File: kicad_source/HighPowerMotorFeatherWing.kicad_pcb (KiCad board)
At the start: 2 copper layers, 100 x 60 mm, 97 parts, among them CN1 ADAFRUIT_FEATHER, P1 WR-TBL_691313710002, P2 WR-TBL_691322310002, P3 WR-TBL_691313710002, P4 WR-TBL_691313710002, Q1 Q_NPN_BEC, Q2 IPD90P03P4L- 04, U1 IFX007T, U2 74xx08, U3 IFX007T, U4 IFX007T, U5 IFX007T, U6 OPA2374AIDCN, U7 OPA2374AIDCN, U8 ADS1015, U9 IFX91041EFJ

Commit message: added manufacturing pdfs
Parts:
- C1, C10, C13, C14, C17, C2, C23, C26, C30, C34, C35, C5, C6, C9: value C_0603 -> 100nF
- C11, C12, C15, C16, C3, C4, C7, C8: value C_0603 -> 220nF
- C18, C21: value 100n -> 100nF
- C19, C20, C25: value CP1_Small -> 47uF 50V
- C22, C24: value C_0603 -> 1nF
- C27: value 220n -> 220nF
- C28, C29: value CP1_Small -> 330uF 6.3V
- C31: value C_0603 -> 22nF
- C33: value 470p -> 470pF
- C36, C37, C38: value 1000u/50V -> 1000uF 50V
- D1: value D_Small -> BAT46W
- D3: value D_Small -> SSA34
- Q1: value Q_NPN_BEC -> 2N7002
- R1, R10, R12, R13, R17, R18, R19, R2, R28, R29, R33, R4, R5, R7, R8, R9: value R_0603 -> 10k
- R11, R14, R3, R6: value R_0603 -> 510
- R16: value R_0603 -> 150k
- R20, R23, R24, R27, R35: value R_0603 -> 2k2
- R21, R22, R25, R26: value R_0603 -> 56k
- R30, R32: value R_0603 -> 1k
- R31: value R_0603 -> DNI
- R34: value R_0603 -> 22k
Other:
- board text added: "Copyright generationmake 2019 see full project documentation at https://github.com/generationmake/HighPowerMotorFeatherWing This documentation describes Open Hardware and is licensed under the CERN OHL v. 1.2. You may redistribute and modify this documentation under the terms of the CERN OHL v.1.2. (http://ohwr.org/cernohl). This documentation is distributed WITHOUT ANY EXPRESS OR IMPLIED WARRANT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"
- board text removed: "Copyright generationmake 2019 see full project documentation at http://arduhmi.generationmake.de This documentation describes Open Hardware and is licensed under the CERN OHL v. 1.2. You may redistribute and modify this documentation under the terms of the CERN OHL v.1.2. (http://ohwr.org/cernohl). This documentation is distributed WITHOUT ANY EXPRESS OR IMPLIED WARRANTY, INCLUDING OF MERCHANTABI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"

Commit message: added mounting instructions
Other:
- board text added: "10x"
- board text added: "6x for heatspreader"

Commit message: added 3D model for Adafruit Feather connector
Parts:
- P2: value WR-TBL_691322310002 -> WR-TBL_ 691322310002

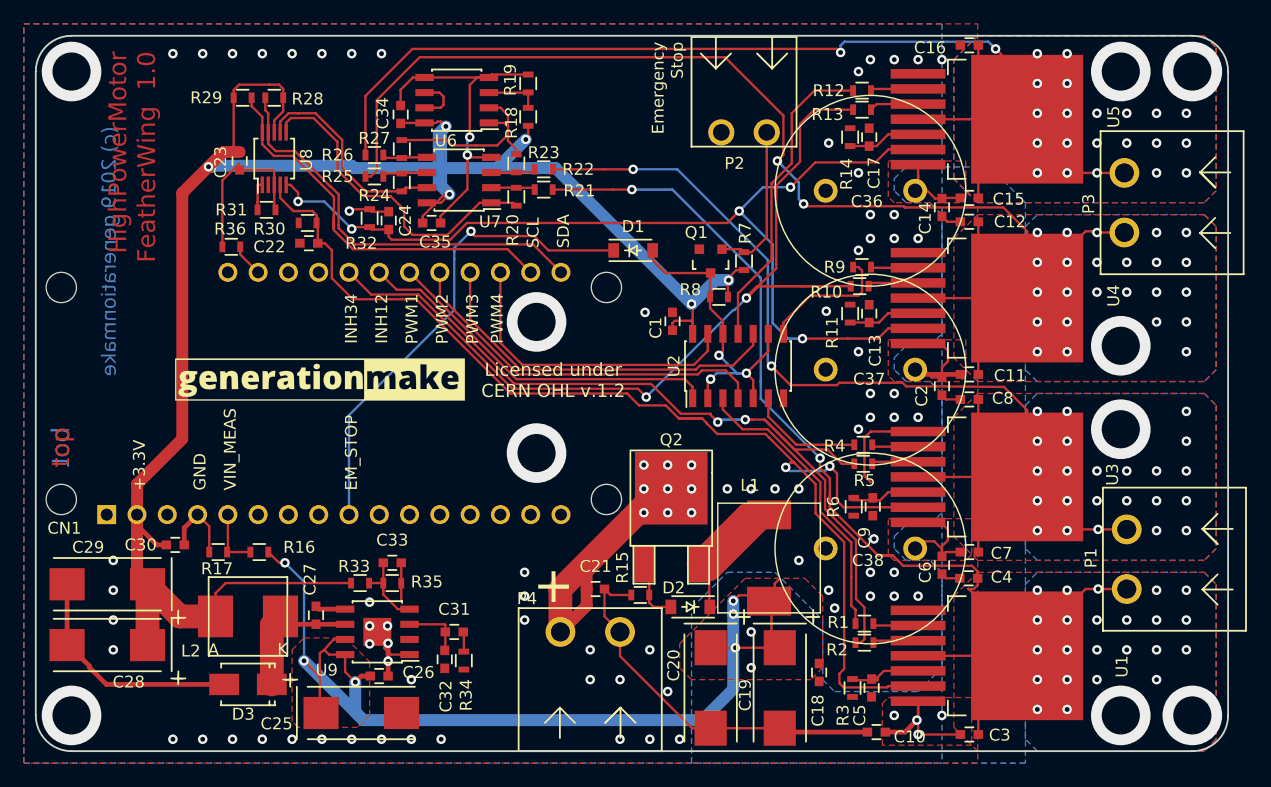
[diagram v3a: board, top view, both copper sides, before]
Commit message: changed mounting holes to parts and generated step file
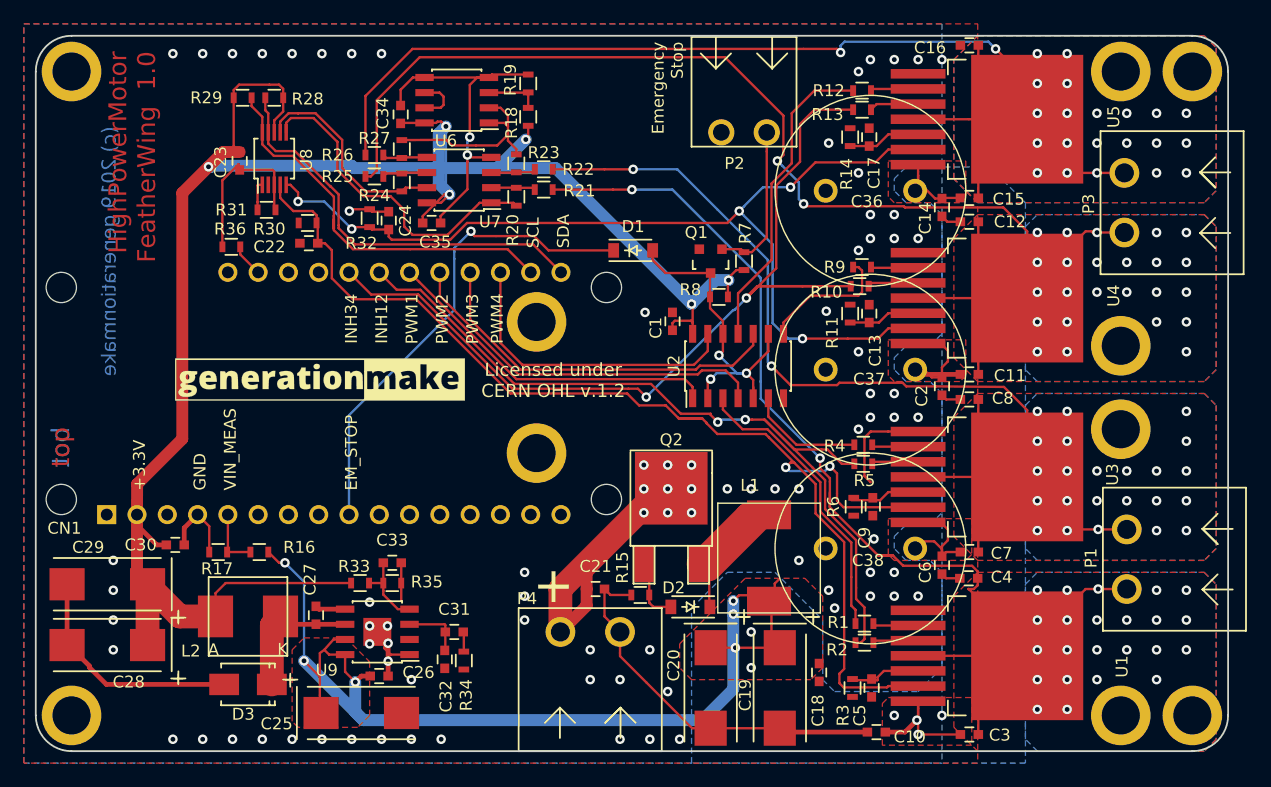
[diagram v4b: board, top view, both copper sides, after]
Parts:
- added MECH1: MHP_3.2_5.0, MECH_mounting_holes:MHP_3.2_5.0, F.Cu at (54.0, 69.0)
- added MECH10: MHP_3.2_5.0, MECH_mounting_holes:MHP_3.2_5.0, F.Cu at (142.0, 123.0)
- added MECH2: MHP_3.2_5.0, MECH_mounting_holes:MHP_3.2_5.0, F.Cu at (54.0, 123.0)
- added MECH3: MHP_3.2_5.0, MECH_mounting_holes:MHP_3.2_5.0, F.Cu at (148.0, 69.0)
- added MECH4: MHP_3.2_5.0, MECH_mounting_holes:MHP_3.2_5.0, F.Cu at (148.0, 123.0)
- added MECH5: MHP_3.2_5.0, MECH_mounting_holes:MHP_3.2_5.0, F.Cu at (93.0, 90.0)
- added MECH6: MHP_3.2_5.0, MECH_mounting_holes:MHP_3.2_5.0, F.Cu at (93.0, 101.0)
- added MECH7: MHP_3.2_5.0, MECH_mounting_holes:MHP_3.2_5.0, F.Cu at (142.0, 69.0)
- added MECH8: MHP_3.2_5.0, MECH_mounting_holes:MHP_3.2_5.0, F.Cu at (142.0, 92.0)
- added MECH9: MHP_3.2_5.0, MECH_mounting_holes:MHP_3.2_5.0, F.Cu at (142.0, 99.0)
- P2: value WR-TBL_ 691322310002 -> WR-TBL_691322310002
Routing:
- net (no net): vias 10 -> 0
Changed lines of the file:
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@@
-(kicad_pcb (version 20171130) (host pcbnew 5.1.5-52549c5~84~ubuntu18.04.1)
+(kicad_pcb (version 20171130) (host pcbnew 5.1.5-52549c5~86~ubuntu18.04.1)
   (general
     (thickness 1.6)
     (drawings 66)
-    (tracks 962)
+    (tracks 952)
     (zones 0)
-    (modules 97)
+    (modules 107)
     (nets 57)
   )
@@
     (solder_mask_min_width 0.25)
     (aux_axis_origin 0 0)
+    (grid_origin 51 126)
     (visible_elements FFFDFF7F)
     (pcbplotparams
@@
       (effects (font (size 1 1) (thickness 0.15)))
     )
-    (fp_text value "WR-TBL_ 691322310002" (at 0 -3.81) (layer F.Fab) hide
+    (fp_text value WR-TBL_691322310002 (at 0 -3.81) (layer F.Fab) hide
       (effects (font (size 1 1) (thickness 0.15)))
     )
@@
     )
   )
+  (module MECH_mounting_holes:MHP_3.2_5.0 (layer F.Cu)
+    (at 54 69)
+    (descr "Mounting hole plated, 3.2mm drill, 5.0mm diameter")
+    (tags "Mounting hole plated, 3.2mm drill, 5.0mm diameter")
+    (fp_text reference MECH1 (at 0 0.5) (layer F.SilkS) hide
+      (effects (font (size 1 1) (thickness 0.15)))
+    )
+    (fp_text value MHP_3.2_5.0 (at 0 -0.5) (layer F.Fab)
+      (effects (font (size 1 1) (thickness 0.15)))
+    )
+    (pad 1 thru_hole circle (at 0 0) (size 5 5) (drill 3.2) (layers *.Cu *.Mask))
+  )
+  (module MECH_mounting_holes:MHP_3.2_5.0 (layer F.Cu)
+    (at 54 123)
+    (descr "Mounting hole plated, 3.2mm drill, 5.0mm diameter")
+    (tags "Mounting hole plated, 3.2mm drill, 5.0mm diameter")
+    (fp_text reference MECH2 (at 0 0.5) (layer F.SilkS) hide
+      (effects (font (size 1 1) (thickness 0.15)))
+    )
+    (fp_text value MHP_3.2_5.0 (at 0 -0.5) (layer F.Fab)
+      (effects (font (size 1 1) (thickness 0.15)))
+    )
+    (pad 1 thru_hole circle (at 0 0) (size 5 5) (drill 3.2) (layers *.Cu *.Mask))
+  )
+  (module MECH_mounting_holes:MHP_3.2_5.0 (layer F.Cu)
+    (at 148 69)
+    (descr "Mounting hole plated, 3.2mm drill, 5.0mm diameter")
+    (tags "Mounting hole plated, 3.2mm drill, 5.0mm diameter")
+    (fp_text reference MECH3 (at 0 0.5) (layer F.SilkS) hide
+      (effects (font (size 1 1) (thickness 0.15)))
+    )
+    (fp_text value MHP_3.2_5.0 (at 0 -0.5) (layer F.Fab)
+      (effects (font (size 1 1) (thickness 0.15)))
+    )
+    (pad 1 thru_hole circle (at 0 0) (size 5 5) (drill 3.2) (layers *.Cu *.Mask))
+  )
+  (module MECH_mounting_holes:MHP_3.2_5.0 (layer F.Cu)
+    (at 148 123)
+    (descr "Mounting hole plated, 3.2mm drill, 5.0mm diameter")
+    (tags "Mounting hole plated, 3.2mm drill, 5.0mm diameter")
+    (fp_text reference MECH4 (at 0 0.5) (layer F.SilkS) hide
+      (effects (font (size 1 1) (thickness 0.15)))
+    )
+    (fp_text value MHP_3.2_5.0 (at 0 -0.5) (layer F.Fab)
+      (effects (font (size 1 1) (thickness 0.15)))
+    )
+    (pad 1 thru_hole circle (at 0 0) (size 5 5) (drill 3.2) (layers *.Cu *.Mask))
+  )
+  (module MECH_mounting_holes:MHP_3.2_5.0 (layer F.Cu)
+    (at 93 90)
+    (descr "Mounting hole plated, 3.2mm drill, 5.0mm diameter")
+    (tags "Mounting hole plated, 3.2mm drill, 5.0mm diameter")
+    (fp_text reference MECH5 (at 0 0.5) (layer F.SilkS) hide
+      (effects (font (size 1 1) (thickness 0.15)))
+    )
+    (fp_text value MHP_3.2_5.0 (at 0 -0.5) (layer F.Fab)
+      (effects (font (size 1 1) (thickness 0.15)))
+    )
+    (pad 1 thru_hole circle (at 0 0) (size 5 5) (drill 3.2) (layers *.Cu *.Mask))
+  )
+  (module MECH_mounting_holes:MHP_3.2_5.0 (layer F.Cu)
+    (at 93 101)
+    (descr "Mounting hole plated, 3.2mm drill, 5.0mm diameter")
+    (tags "Mounting hole plated, 3.2mm drill, 5.0mm diameter")
+    (fp_text reference MECH6 (at 0 0.5) (layer F.SilkS) hide
+      (effects (font (size 1 1) (thickness 0.15)))
+    )
+    (fp_text value MHP_3.2_5.0 (at 0 -0.5) (layer F.Fab)
+      (effects (font (size 1 1) (thickness 0.15)))
+    )
+    (pad 1 thru_hole circle (at 0 0) (size 5 5) (drill 3.2) (layers *.Cu *.Mask))
+  )
+  (module MECH_mounting_holes:MHP_3.2_5.0 (layer F.Cu)
+    (at 142 69)
+    (descr "Mounting hole plated, 3.2mm drill, 5.0mm diameter")
+    (tags "Mounting hole plated, 3.2mm drill, 5.0mm diameter")
+    (fp_text reference MECH7 (at 0 0.5) (layer F.SilkS) hide
+      (effects (font (size 1 1) (thickness 0.15)))
+    )
+    (fp_text value MHP_3.2_5.0 (at 0 -0.5) (layer F.Fab)
+      (effects (font (size 1 1) (thickness 0.15)))
+    )
+    (pad 1 thru_hole circle (at 0 0) (size 5 5) (drill 3.2) (layers *.Cu *.Mask))
+  )
+  (module MECH_mounting_holes:MHP_3.2_5.0 (layer F.Cu)
+    (at 142 92)
+    (descr "Mounting hole plated, 3.2mm drill, 5.0mm diameter")
+    (tags "Mounting hole plated, 3.2mm drill, 5.0mm diameter")
+    (fp_text reference MECH8 (at 0 0.5) (layer F.SilkS) hide
+      (effects (font (size 1 1) (thickness 0.15)))
+    )
+    (fp_text value MHP_3.2_5.0 (at 0 -0.5) (layer F.Fab)
+      (effects (font (size 1 1) (thickness 0.15)))
+    )
+    (pad 1 thru_hole circle (at 0 0) (size 5 5) (drill 3.2) (layers *.Cu *.Mask))
+  )
+  (module MECH_mounting_holes:MHP_3.2_5.0 (layer F.Cu)
+    (at 142 99)
+    (descr "Mounting hole plated, 3.2mm drill, 5.0mm diameter")
+    (tags "Mounting hole plated, 3.2mm drill, 5.0mm diameter")
+    (fp_text reference MECH9 (at 0 0.5) (layer F.SilkS) hide
+      (effects (font (size 1 1) (thickness 0.15)))
+    )
+    (fp_text value MHP_3.2_5.0 (at 0 -0.5) (layer F.Fab)
+      (effects (font (size 1 1) (thickness 0.15)))
+    )
+    (pad 1 thru_hole circle (at 0 0) (size 5 5) (drill 3.2) (layers *.Cu *.Mask))
+  )
+  (module MECH_mounting_holes:MHP_3.2_5.0 (layer F.Cu)
+    (at 142 123)
+    (descr "Mounting hole plated, 3.2mm drill, 5.0mm diameter")
+    (tags "Mounting hole plated, 3.2mm drill, 5.0mm diameter")
+    (fp_text reference MECH10 (at 0 0.5) (layer F.SilkS) hide
+      (effects (font (size 1 1) (thickness 0.15)))
+    )
+    (fp_text value MHP_3.2_5.0 (at 0 -0.5) (layer F.Fab)
+      (effects (font (size 1 1) (thickness 0.15)))
+    )
+    (pad 1 thru_hole circle (at 0 0) (size 5 5) (drill 3.2) (layers *.Cu *.Mask))
+  )
   (gr_line (start 125.4 96.2) (end 140.6 121.3) (layer Eco1.User) (width 0.15))
   (gr_line (start 125.6 95) (end 140.8 70.6) (layer Eco1.User) (width 0.15))
@@
   (gr_line (start 148 126) (end 54 126) (angle 90) (layer Edge.Cuts) (width 0.15))
   (gr_line (start 54 66) (end 148 66) (angle 90) (layer Edge.Cuts) (width 0.15))
-  (via (at 148 123) (size 5) (drill 3.2) (layers F.Cu B.Cu) (net 0))
-  (via (at 148 69) (size 5) (drill 3.2) (layers F.Cu B.Cu) (net 0))
-  (via (at 54 69) (size 5) (drill 3.2) (layers F.Cu B.Cu) (net 0))
-  (via (at 54 123) (size 5) (drill 3.2) (layers F.Cu B.Cu) (net 0))
-  (via (at 142 123) (size 5) (drill 3.2) (layers F.Cu B.Cu) (net 0))
-  (via (at 142 99) (size 5) (drill 3.2) (layers F.Cu B.Cu) (net 0) (status 40000))
-  (via (at 142 92) (size 5) (drill 3.2) (layers F.Cu B.Cu) (net 0))
-  (via (at 142 69) (size 5) (drill 3.2) (layers F.Cu B.Cu) (net 0))
-  (via (at 93 90) (size 5) (drill 3.2) (layers F.Cu B.Cu) (net 0))
-  (via (at 93 101) (size 5) (drill 3.2) (layers F.Cu B.Cu) (net 0) (status 40000))
   (via (at 79 117) (size 0.8) (drill 0.4) (layers F.Cu B.Cu) (net 1) (status 30))
   (via (at 80.5 115.5) (size 0.8) (drill 0.4) (layers F.Cu B.Cu) (net 1) (status 30))
